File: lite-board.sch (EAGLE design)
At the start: 42 parts, among them IC1 LM324D, IC2 LM324D, IC3 LM324D, IC4 LM324D, IC5 LM324D, IC6 LM324D

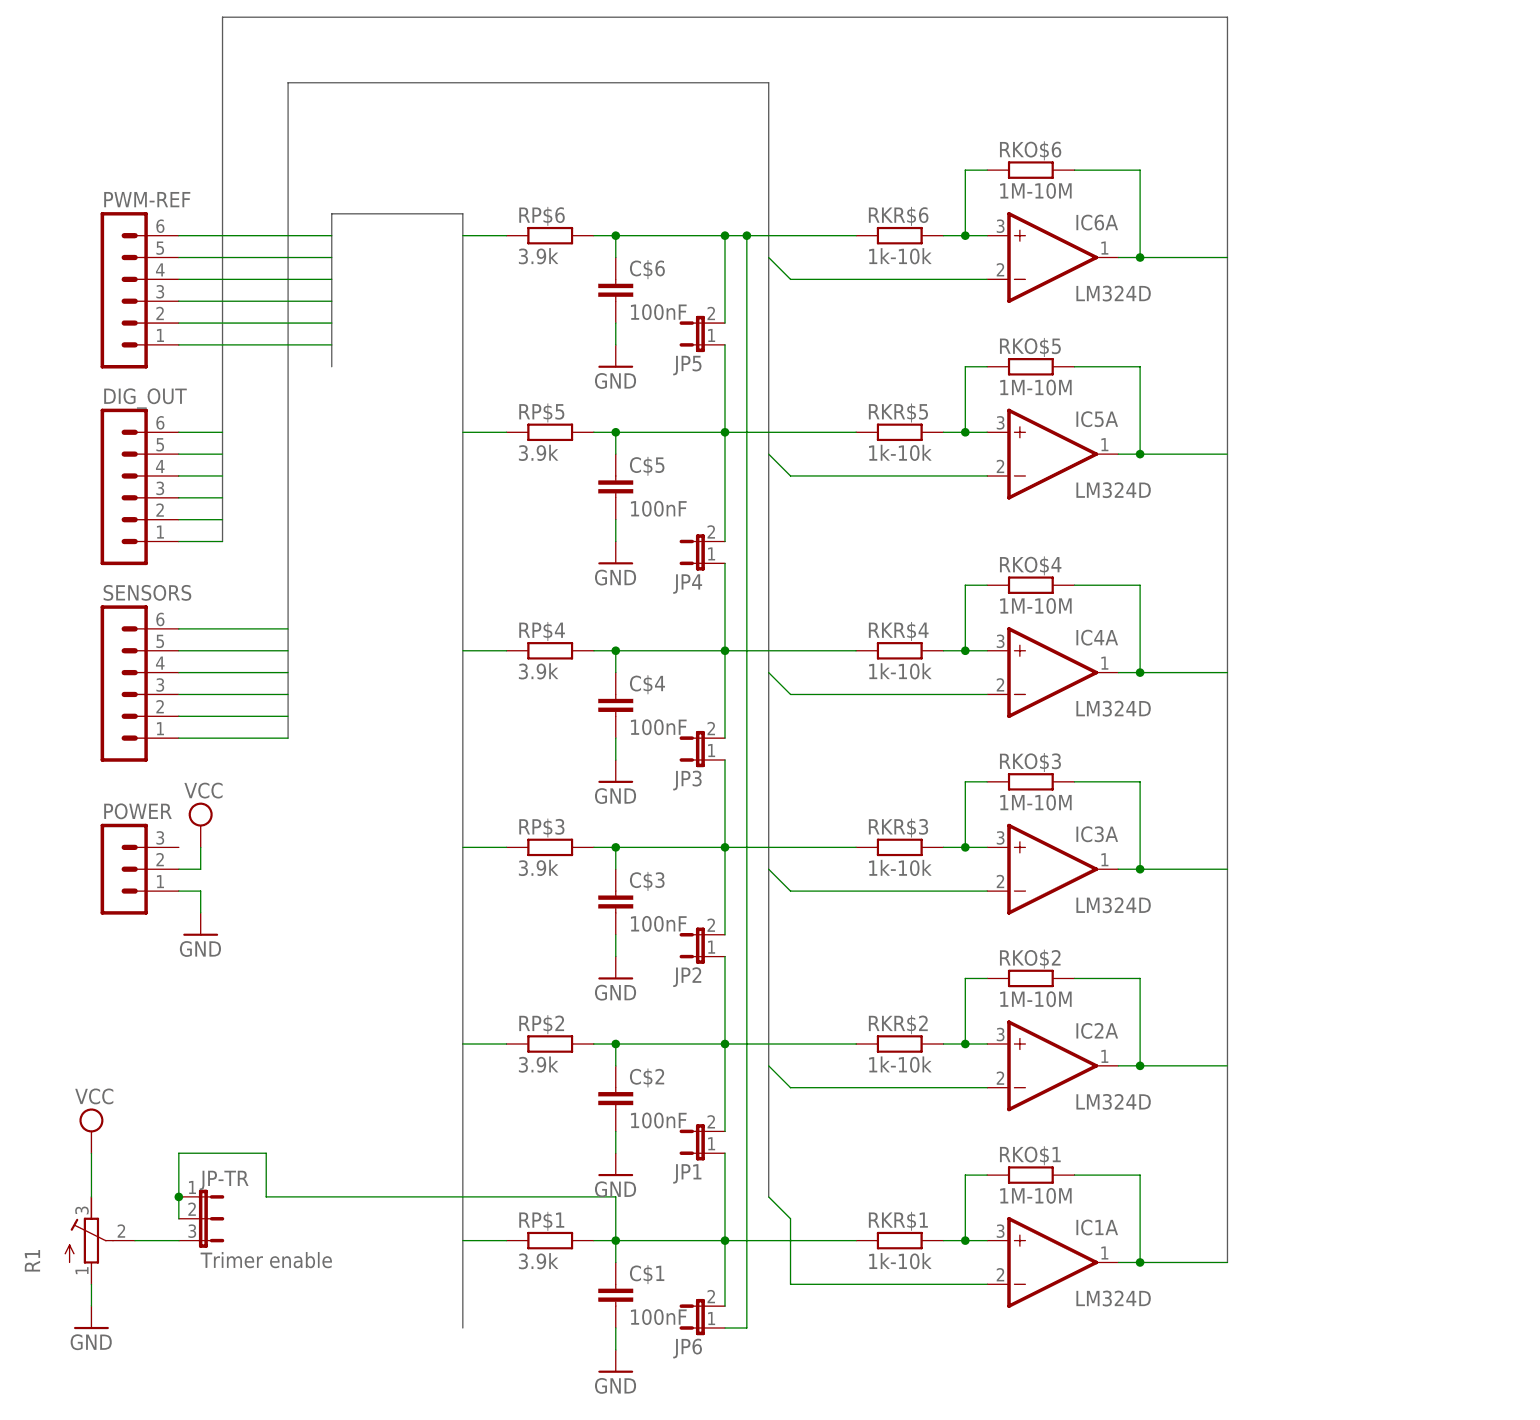
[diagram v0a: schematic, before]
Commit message: OAmp package changes
* I used more OAmpps per packages

* Connected OAmps to power supply
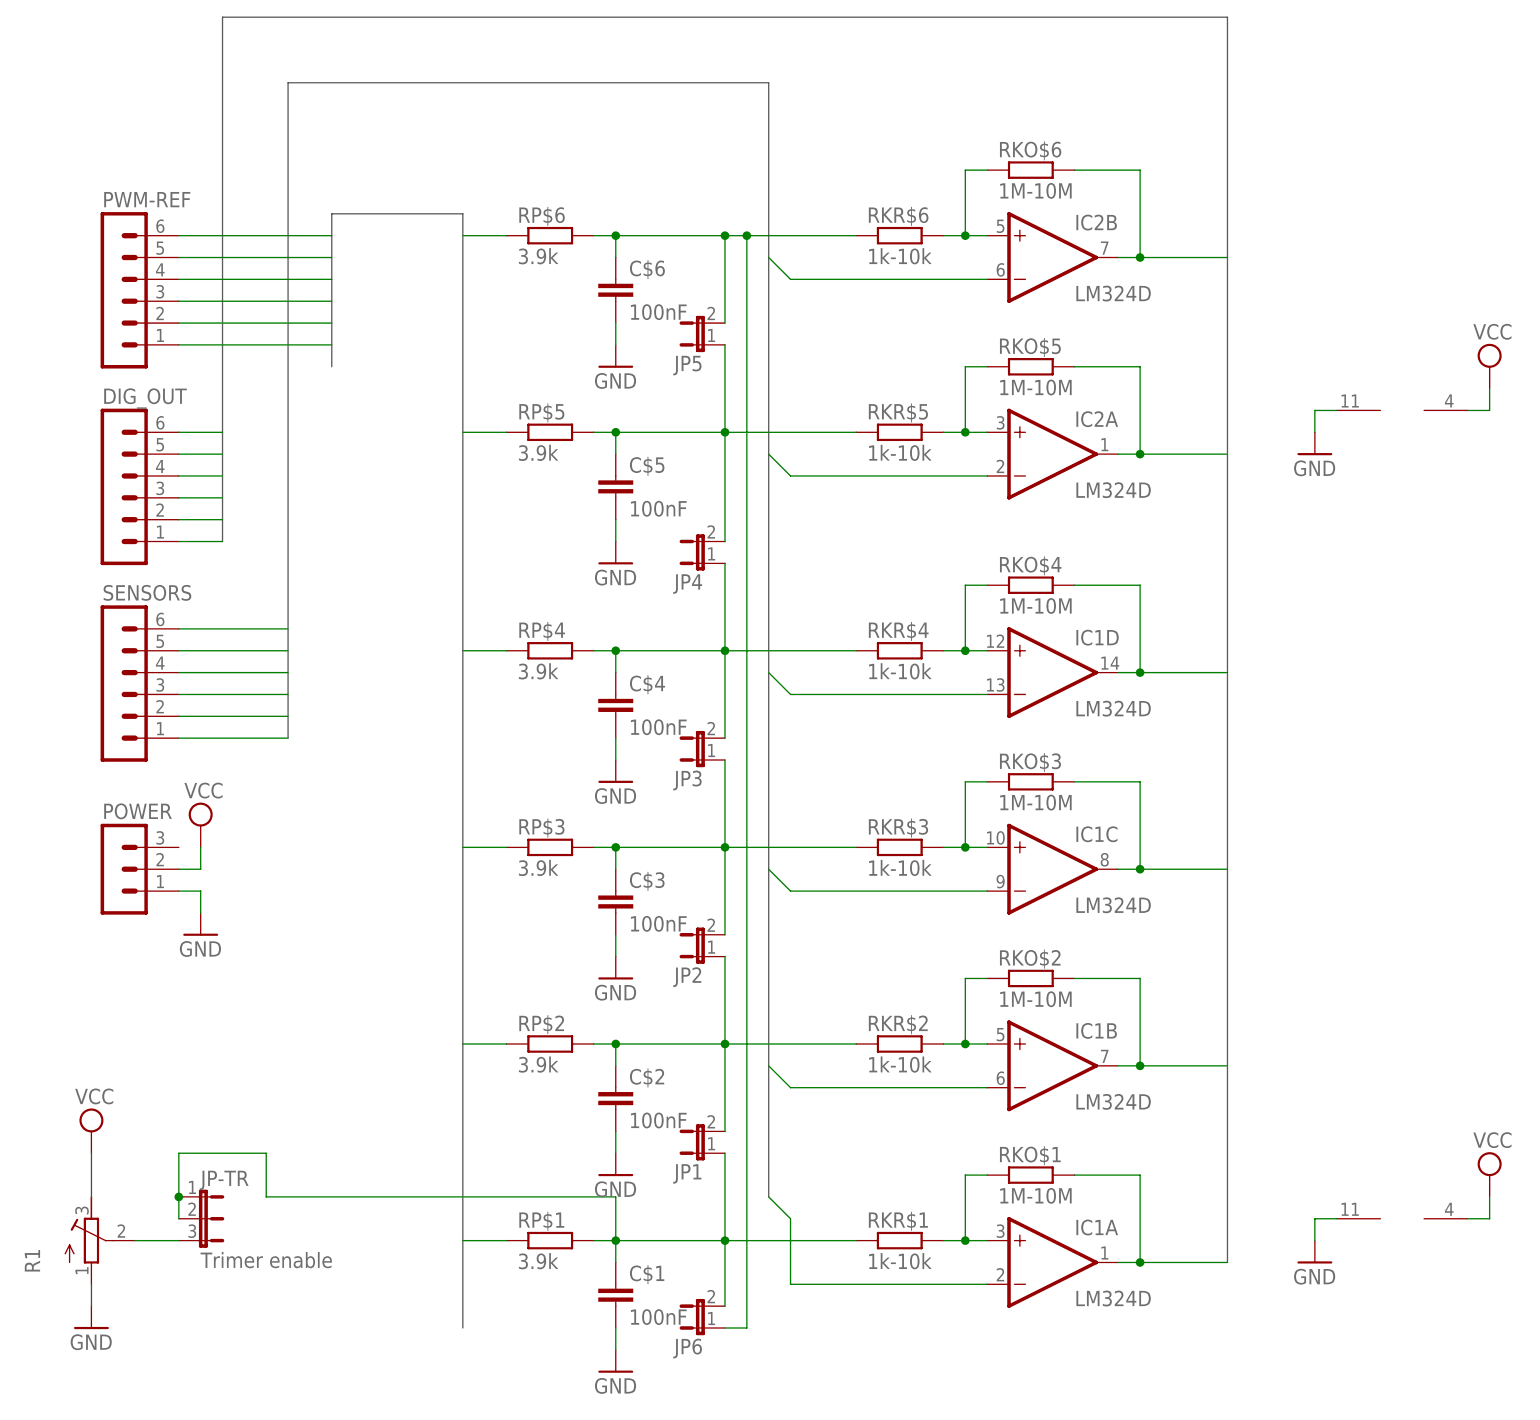
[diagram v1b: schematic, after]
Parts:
- removed IC3, IC4, IC5, IC6: LM324D, linear:LM324D
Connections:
- removed net N$16: IC6A.+IN, RKO$6.1, RKR$6.2
- new net N$3: IC2B.+IN, RKO$6.1, RKR$6.2
- net BOUT2: now also IC1B.OUT; no longer IC2A.OUT
- net BOUT3: now also IC1C.OUT; no longer IC3A.OUT
- net BOUT4: now also IC1D.OUT; no longer IC4A.OUT
- net BOUT5: now also IC2A.OUT; no longer IC5A.OUT
- net BOUT6: now also IC2B.OUT; no longer IC6A.OUT
- net BSENZ2: now also IC1B.-IN; no longer IC2A.-IN
- net BSENZ3: now also IC1C.-IN; no longer IC3A.-IN
- net BSENZ4: now also IC1D.-IN; no longer IC4A.-IN
- net BSENZ5: now also IC2A.-IN; no longer IC5A.-IN
- net BSENZ6: now also IC2B.-IN; no longer IC6A.-IN
- net GND: now also IC1P.V-, IC2P.V-
- net N$10: now also IC1D.+IN; no longer IC4A.+IN
- net N$13: now also IC2A.+IN; no longer IC5A.+IN
- net N$4: now also IC1B.+IN; no longer IC2A.+IN
- net N$7: now also IC1C.+IN; no longer IC3A.+IN
- net VCC: now also IC1P.V+, IC2P.V+
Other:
- moved on the sheet: IC2A

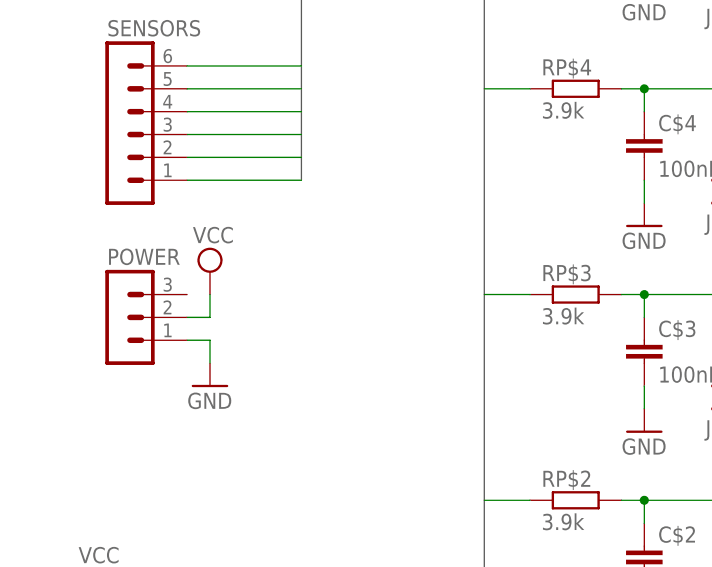
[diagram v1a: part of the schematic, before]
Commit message: added diode to protect input
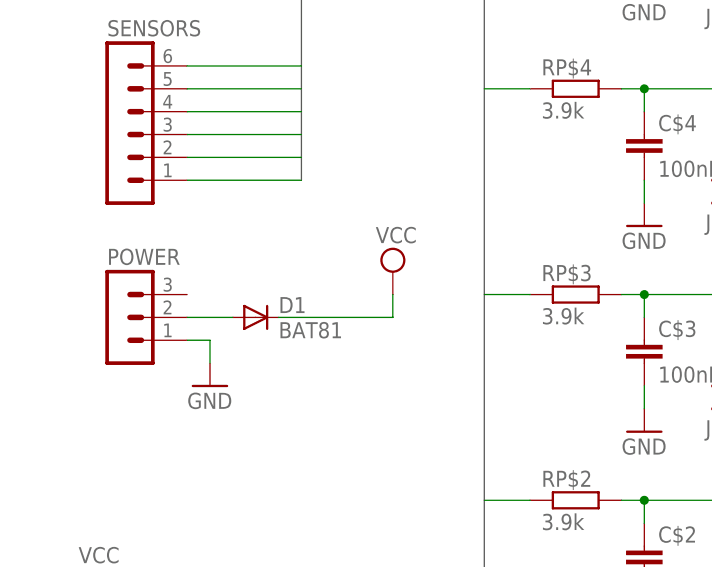
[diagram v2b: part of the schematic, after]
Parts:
- added D1: BAT81, diode:BAT81
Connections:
- new net N$5: D1.A, POWER.2
- net VCC: now also D1.C; no longer POWER.2
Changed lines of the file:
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@@
 <grid distance="0.1" unitdist="inch" unit="inch" style="lines" multiple="1" display="no" altdistance="0.01" altunitdist="inch" altunit="inch"/>
 <layers>
-<layer number="1" name="Top" color="4" fill="1" visible="yes" active="no"/>
-<layer number="16" name="Bottom" color="1" fill="1" visible="yes" active="no"/>
-<layer number="17" name="Pads" color="2" fill="1" visible="yes" active="no"/>
-<layer number="18" name="Vias" color="2" fill="1" visible="yes" active="no"/>
-<layer number="19" name="Unrouted" color="6" fill="1" visible="yes" active="no"/>
-<layer number="20" name="Dimension" color="15" fill="1" visible="yes" active="no"/>
-<layer number="21" name="tPlace" color="7" fill="1" visible="yes" active="no"/>
-<layer number="22" name="bPlace" color="7" fill="1" visible="yes" active="no"/>
-<layer number="23" name="tOrigins" color="15" fill="1" visible="yes" active="no"/>
-<layer number="24" name="bOrigins" color="15" fill="1" visible="yes" active="no"/>
-<layer number="25" name="tNames" color="7" fill="1" visible="yes" active="no"/>
-<layer number="26" name="bNames" color="7" fill="1" visible="yes" active="no"/>
-<layer number="27" name="tValues" color="7" fill="1" visible="yes" active="no"/>
-<layer number="28" name="bValues" color="7" fill="1" visible="yes" active="no"/>
+<layer number="1" name="Top" color="4" fill="1" visible="no" active="no"/>
+<layer number="16" name="Bottom" color="1" fill="1" visible="no" active="no"/>
+<layer number="17" name="Pads" color="2" fill="1" visible="no" active="no"/>
+<layer number="18" name="Vias" color="2" fill="1" visible="no" active="no"/>
+<layer number="19" name="Unrouted" color="6" fill="1" visible="no" active="no"/>
+<layer number="20" name="Dimension" color="15" fill="1" visible="no" active="no"/>
+<layer number="21" name="tPlace" color="7" fill="1" visible="no" active="no"/>
+<layer number="22" name="bPlace" color="7" fill="1" visible="no" active="no"/>
+<layer number="23" name="tOrigins" color="15" fill="1" visible="no" active="no"/>
+<layer number="24" name="bOrigins" color="15" fill="1" visible="no" active="no"/>
+<layer number="25" name="tNames" color="7" fill="1" visible="no" active="no"/>
+<layer number="26" name="bNames" color="7" fill="1" visible="no" active="no"/>
+<layer number="27" name="tValues" color="7" fill="1" visible="no" active="no"/>
+<layer number="28" name="bValues" color="7" fill="1" visible="no" active="no"/>
 <layer number="29" name="tStop" color="7" fill="3" visible="no" active="no"/>
 <layer number="30" name="bStop" color="7" fill="6" visible="no" active="no"/>
@@
 <layer number="35" name="tGlue" color="7" fill="4" visible="no" active="no"/>
 <layer number="36" name="bGlue" color="7" fill="5" visible="no" active="no"/>
-<layer number="37" name="tTest" color="7" fill="1" visible="yes" active="no"/>
-<layer number="38" name="bTest" color="7" fill="1" visible="yes" active="no"/>
+<layer number="37" name="tTest" color="7" fill="1" visible="no" active="no"/>
+<layer number="38" name="bTest" color="7" fill="1" visible="no" active="no"/>
 <layer number="39" name="tKeepout" color="4" fill="11" visible="no" active="no"/>
 <layer number="40" name="bKeepout" color="1" fill="11" visible="no" active="no"/>
@@
 <layer number="44" name="Drills" color="7" fill="1" visible="no" active="no"/>
 <layer number="45" name="Holes" color="7" fill="1" visible="no" active="no"/>
-<layer number="46" name="Milling" color="3" fill="1" visible="yes" active="no"/>
-<layer number="47" name="Measures" color="7" fill="1" visible="yes" active="no"/>
-<layer number="48" name="Document" color="7" fill="1" visible="yes" active="no"/>
-<layer number="49" name="Reference" color="7" fill="1" visible="yes" active="no"/>
-<layer number="51" name="tDocu" color="7" fill="1" visible="yes" active="no"/>
-<layer number="52" name="bDocu" color="7" fill="1" visible="yes" active="no"/>
+<layer number="46" name="Milling" color="3" fill="1" visible="no" active="no"/>
+<layer number="47" name="Measures" color="7" fill="1" visible="no" active="no"/>
+<layer number="48" name="Document" color="7" fill="1" visible="no" active="no"/>
+<layer number="49" name="Reference" color="7" fill="1" visible="no" active="no"/>
+<layer number="51" name="tDocu" color="7" fill="1" visible="no" active="no"/>
+<layer number="52" name="bDocu" color="7" fill="1" visible="no" active="no"/>
 <layer number="91" name="Nets" color="2" fill="1" visible="yes" active="yes"/>
 <layer number="92" name="Busses" color="1" fill="1" visible="yes" active="yes"/>
@@
 <layer number="97" name="Info" color="7" fill="1" visible="yes" active="yes"/>
 <layer number="98" name="Guide" color="6" fill="1" visible="yes" active="yes"/>
+<layer number="99" name="SpiceOrder" color="5" fill="1" visible="yes" active="yes"/>
 </layers>
 <schematic xreflabel="%F%N/%S.%C%R" xrefpart="/%S.%C%R">
@@
 <part name="GND10" library="supply1" deviceset="GND" device=""/>
 <part name="SUPPLY4" library="supply2" deviceset="VCC" device=""/>
+<part name="D1" library="diode" deviceset="BAT81" device=""/>
 </parts>
 <sheets>
@@
 <instance part="POWER" gate="G$1" x="10.16" y="71.12"/>
 <instance part="GND8" gate="1" x="20.32" y="63.5"/>
-<instance part="SUPPLY2" gate="G$1" x="20.32" y="76.2"/>
+<instance part="SUPPLY2" gate="G$1" x="40.64" y="76.2"/>
 <instance part="IC1" gate="B" x="119.38" y="48.26"/>
 <instance part="IC1" gate="C" x="119.38" y="71.12"/>
@@
 <instance part="GND10" gate="1" x="149.86" y="119.38"/>
 <instance part="SUPPLY4" gate="G$1" x="170.18" y="129.54"/>
+<instance part="D1" gate="1" x="25.4" y="71.12"/>
 </instances>
 <busses>
@@
 </segment>
 <segment>
-<pinref part="SUPPLY2" gate="G$1" pin="VCC"/>
-<wire x1="20.32" y1="73.66" x2="20.32" y2="71.12" width="0.1524" layer="91"/>
-<pinref part="POWER" gate="G$1" pin="2"/>
-<wire x1="20.32" y1="71.12" x2="17.78" y2="71.12" width="0.1524" layer="91"/>
-</segment>
-<segment>
 <pinref part="IC1" gate="P" pin="V+"/>
 <wire x1="167.64" y1="30.48" x2="170.18" y2="30.48" width="0.1524" layer="91"/>
@@
 <pinref part="SUPPLY4" gate="G$1" pin="VCC"/>
 <wire x1="170.18" y1="124.46" x2="170.18" y2="127" width="0.1524" layer="91"/>
+</segment>
+<segment>
+<pinref part="SUPPLY2" gate="G$1" pin="VCC"/>
+<wire x1="40.64" y1="71.12" x2="40.64" y2="73.66" width="0.1524" layer="91"/>
+<pinref part="D1" gate="1" pin="C"/>
+<wire x1="27.94" y1="71.12" x2="40.64" y2="71.12" width="0.1524" layer="91"/>
 </segment>
 </net>
@@
 </segment>
 </net>
+<net name="N$5" class="0">
+<segment>
+<pinref part="POWER" gate="G$1" pin="2"/>
+<pinref part="D1" gate="1" pin="A"/>
+<wire x1="17.78" y1="71.12" x2="22.86" y2="71.12" width="0.1524" layer="91"/>
+</segment>
+</net>
 </nets>
 </sheet>
 </sheets>
+<errors>
+</errors>
 </schematic>
 </drawing>
